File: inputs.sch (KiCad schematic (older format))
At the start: 63 parts, among them J21 Conn_01x02, J22 Conn_01x02, J23 Conn_01x02, J24 Conn_01x03, J25 Conn_01x03, J26 Conn_01x03, J27 Conn_01x03, J28 Conn_01x03, J29 Conn_01x03, J31 Conn_01x04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

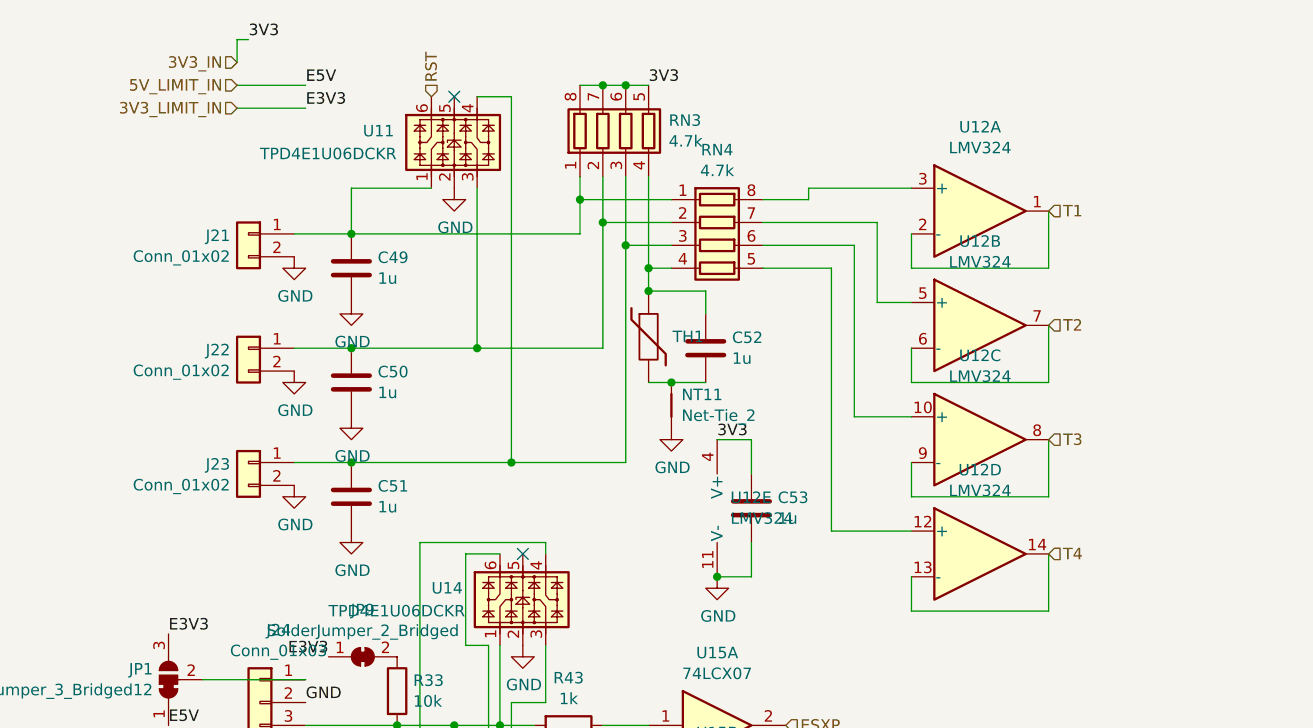
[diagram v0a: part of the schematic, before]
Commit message: Switch ADC opamp to 5V Add 4.7k series resistors (RN9) to thermistor inputs. Add 10k pulldowns (RN8) to FET gate driver inputs.
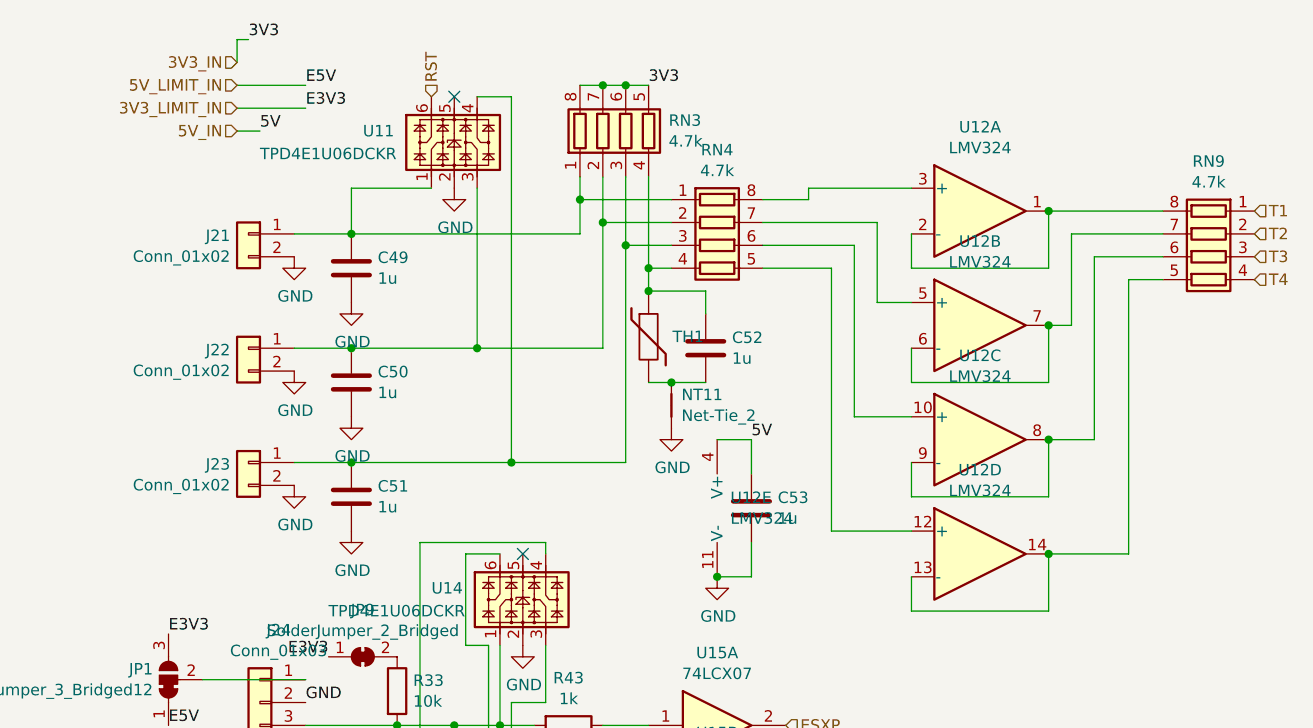
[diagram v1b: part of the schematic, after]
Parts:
- added RN9: 4.7k, Resistor_SMD:R_Array_Concave_4x0603, symbol Device:R_Pack04
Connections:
- net 3V3_IN: no longer C53.1, U12.4 (V+)
- net T1: now also RN9.1 (R1.1); no longer U12.1, U12.2 (-)
- net T2: now also RN9.2 (R2.1); no longer U12.6 (-), U12.7
- net T3: now also RN9.3 (R3.1); no longer U12.8, U12.9 (-)
- net T4: now also RN9.4 (R4.1); no longer U12.13 (-), U12.14
- new net: RN9.8 (R1.2), U12.1, U12.2 (-)
- new net: RN9.7 (R2.2), U12.6 (-), U12.7
- new net: RN9.6 (R3.2), U12.8, U12.9 (-)
- new net: RN9.5 (R4.2), U12.13 (-), U12.14
- new net 5V_IN: C53.1, U12.4 (V+)
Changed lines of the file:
@@
 Text Label 3850 800  0    50   ~ 0
 3V3
-Text Label 4150 2350 0    50   ~ 0
-3V3
-Text HLabel 5600 1350 2    50   Input ~ 0
+Text HLabel 6500 1350 2    50   Input ~ 0
 T1
-Text HLabel 5600 1850 2    50   Input ~ 0
+Text HLabel 6500 1450 2    50   Input ~ 0
 T2
-Text HLabel 5600 2350 2    50   Input ~ 0
+Text HLabel 6500 1550 2    50   Input ~ 0
 T3
-Text HLabel 5600 2850 2    50   Input ~ 0
+Text HLabel 6500 1650 2    50   Input ~ 0
 T4
 $Comp
@@
 Wire Wire Line
 	2050 900  2350 900
+Text Label 4300 2350 0    50   ~ 0
+5V
+Text HLabel 2050 1000 0    50   Input ~ 0
+5V_IN
+Text Label 2150 1000 0    50   ~ 0
+5V
+Wire Wire Line
+	2150 1000 2050 1000
+$Comp
+L Device:R_Pack04 RN9
+U 1 1 61C42B19
+P 6300 1550
+F 0 "RN9" V 5883 1550 50  0000 C CNN
+F 1 "4.7k" V 5974 1550 50  0000 C CNN
+F 2 "Resistor_SMD:R_Array_Concave_4x0603" V 6575 1550 50  0001 C CNN
+F 3 "~" H 6300 1550 50  0001 C CNN
+	1    6300 1550
+	0    -1   1    0
+$EndComp
+Wire Wire Line
+	6100 1350 5600 1350
+Connection ~ 5600 1350
+Wire Wire Line
+	6100 1450 5700 1450
+Wire Wire Line
+	5700 1450 5700 1850
+Wire Wire Line
+	5700 1850 5600 1850
+Connection ~ 5600 1850
+Wire Wire Line
+	6100 1550 5800 1550
+Wire Wire Line
+	5800 1550 5800 2350
+Wire Wire Line
+	5800 2350 5600 2350
+Connection ~ 5600 2350
+Wire Wire Line
+	6100 1650 5950 1650
+Wire Wire Line
+	5950 1650 5950 2850
+Wire Wire Line
+	5950 2850 5600 2850
+Connection ~ 5600 2850
 $EndSCHEMATC

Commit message: Revision3 - Fix 5V cascading problem, change ADC opamp supply to 5V, add comparator to probe input, pulldown FETs when their MCU pins float.
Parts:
- added R97: 8.2k, Resistor_SMD:R_0402_1005Metric, symbol Device:R
- added R98: 1k, Resistor_SMD:R_0402_1005Metric, symbol Device:R
- added U24: LMV331, Package_TO_SOT_SMD:SOT-23-5, symbol Comparator:LMV331
- JP7: footprint Jumper:SolderJumper-2_P1.3mm_Bridged2Bar_RoundedPad1.0x1.5mm -> Jumper:SolderJumper-2_P1.3mm_Open_RoundedPad1.0x1.5mm; symbol Jumper:SolderJumper_2_Bridged -> Jumper:SolderJumper_2_Open
- R47: value 5.1k -> 7.1k
- R48: value 10k -> 1k
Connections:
- net 3V3_IN: now also R97.2, U24.5 (V+)
- net GND: now also R98.1, U24.2 (V-)
- net PROBE: now also U24.4; no longer R50.1
- net at C60.1, J31.4 (Pin_4), R34.2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: no longer U13.3
- new net: R50.1, U24.1 (+)
- new net: R97.1, R98.2, U24.3 (-)
- no-connect marks 4 -> 5
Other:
- note added: "Set comparator threshold to 0.359V.\nThe output is 3.3V if input pin is between 2.9V and 26V (nominal 24V).\nThe output is 0V if input pin is below 2.9V."
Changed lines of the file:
@@
 $EndComp
 $Comp
-L Jumper:SolderJumper_2_Bridged JP7
+L Jumper:SolderJumper_2_Open JP7
 U 1 1 6154AF0A
 P 2400 7550
 F 0 "JP7" H 2400 7755 50  0000 C CNN
 F 1 "SolderJumper_2_Bridged" H 2400 7664 50  0000 C CNN
-F 2 "Jumper:SolderJumper-2_P1.3mm_Bridged2Bar_RoundedPad1.0x1.5mm" H 2400 7550 50  0001 C CNN
+F 2 "Jumper:SolderJumper-2_P1.3mm_Open_RoundedPad1.0x1.5mm" H 2400 7550 50  0001 C CNN
 F 3 "~" H 2400 7550 50  0001 C CNN
 	1    2400 7550
@@
 	2350 7250 2550 7250
 Connection ~ 2550 7250
-Wire Wire Line
-	2550 7250 2650 7250
 Wire Wire Line
 	2350 6150 2400 6150
@@
 Wire Wire Line
 	2400 6150 2750 6150
-Wire Wire Line
-	2650 6700 2650 7250
-Connection ~ 2650 7250
-Wire Wire Line
-	2650 7250 3000 7250
 NoConn ~ 2550 6300
 NoConn ~ 2450 6300
@@
 Text HLabel 4450 5000 2    50   Input ~ 0
 ESZP
-Text HLabel 4350 7250 2    50   Input ~ 0
+Text HLabel 5900 7150 2    50   Input ~ 0
 PROBE
 Text HLabel 4450 5350 2    50   Input ~ 0
@@
 P 3300 7250
 F 0 "R47" V 3093 7250 50  0000 C CNN
-F 1 "5.1k" V 3184 7250 50  0000 C CNN
+F 1 "7.1k" V 3184 7250 50  0000 C CNN
 F 2 "Resistor_SMD:R_0402_1005Metric" V 3230 7250 50  0001 C CNN
 F 3 "~" H 3300 7250 50  0001 C CNN
@@
 P 3450 7400
 F 0 "R48" H 3380 7354 50  0000 R CNN
-F 1 "10k" H 3380 7445 50  0000 R CNN
+F 1 "1k" H 3380 7445 50  0000 R CNN
 F 2 "Resistor_SMD:R_0402_1005Metric" V 3380 7400 50  0001 C CNN
 F 3 "~" H 3450 7400 50  0001 C CNN
@@
 	5950 2850 5600 2850
 Connection ~ 5600 2850
+$Comp
+L Comparator:LMV331 U24
+U 1 1 61E69E41
+P 5600 7150
+F 0 "U24" H 5650 7300 50  0000 L CNN
+F 1 "LMV331" H 5650 7000 50  0000 L CNN
+F 2 "Package_TO_SOT_SMD:SOT-23-5" H 5600 7250 50  0001 C CNN
+F 3 "http://www.ti.com/lit/ds/symlink/lmv331.pdf" H 5600 7350 50  0001 C CNN
+	1    5600 7150
+	1    0    0    -1
+$EndComp
+Text Label 5500 6850 0    50   ~ 0
+3V3
+$Comp
+L power:GND #PWR074
+U 1 1 61E862CC
+P 5500 7450
+F 0 "#PWR074" H 5500 7200 50  0001 C CNN
+F 1 "GND" H 5505 7277 50  0000 C CNN
+F 2 "" H 5500 7450 50  0001 C CNN
+F 3 "" H 5500 7450 50  0001 C CNN
+	1    5500 7450
+	1    0    0    -1
+$EndComp
+Wire Wire Line
+	5300 7050 4350 7050
+Wire Wire Line
+	4350 7050 4350 7250
+Text Label 4600 7250 2    50   ~ 0
+3V3
+$Comp
+L Device:R R97
+U 1 1 61E947D0
+P 4750 7250
+F 0 "R97" V 4543 7250 50  0000 C CNN
+F 1 "8.2k" V 4634 7250 50  0000 C CNN
+F 2 "Resistor_SMD:R_0402_1005Metric" V 4680 7250 50  0001 C CNN
+F 3 "~" H 4750 7250 50  0001 C CNN
+	1    4750 7250
+	0    1    1    0
+$EndComp
+$Comp
+L Device:R R98
+U 1 1 61E9639D
+P 4900 7400
+F 0 "R98" H 4830 7354 50  0000 R CNN
+F 1 "1k" H 4830 7445 50  0000 R CNN
+F 2 "Resistor_SMD:R_0402_1005Metric" V 4830 7400 50  0001 C CNN
+F 3 "~" H 4900 7400 50  0001 C CNN
+	1    4900 7400
+	-1   0    0    1
+$EndComp
+$Comp
+L power:GND #PWR073
+U 1 1 61E96E18
+P 4900 7550
+F 0 "#PWR073" H 4900 7300 50  0001 C CNN
+F 1 "GND" H 4905 7377 50  0000 C CNN
+F 2 "" H 4900 7550 50  0001 C CNN
+F 3 "" H 4900 7550 50  0001 C CNN
+	1    4900 7550
+	1    0    0    -1
+$EndComp
+Wire Wire Line
+	5300 7250 4900 7250
+Connection ~ 4900 7250
+Wire Wire Line
+	2550 7250 3000 7250
+NoConn ~ 2650 6700
+Text Notes 4150 6750 0    50   ~ 0
+Set comparator threshold to 0.359V.\nThe output is 3.3V if input pin is between 2.9V and 26V (nominal 24V).\nThe output is 0V if input pin is below 2.9V.
 $EndSCHEMATC
